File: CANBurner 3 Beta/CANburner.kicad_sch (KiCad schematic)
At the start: 5 parts, among them J1 Conn_02x04_Odd_Even

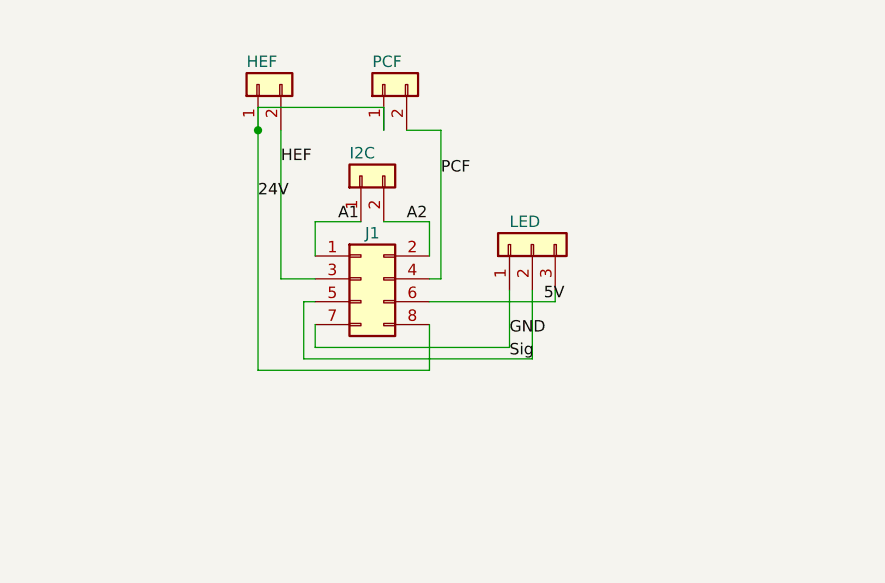
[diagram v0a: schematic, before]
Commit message: Rename KiCAD project files to CANburner
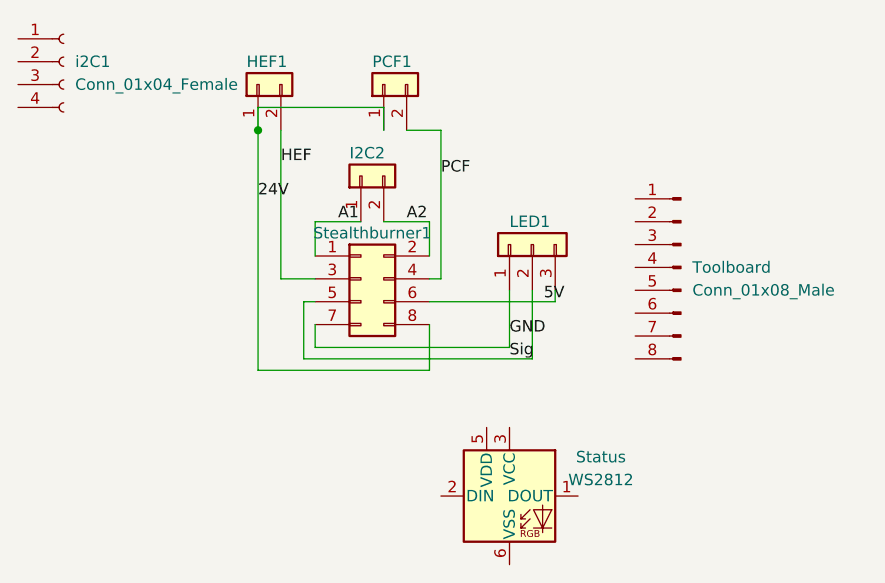
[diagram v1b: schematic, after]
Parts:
- added Status: WS2812, LED_SMD:LED_WS2812_PLCC6_5.0x5.0mm_P1.6mm, symbol LED:WS2812
- added Toolboard: Conn_01x08_Male, Connector_JST:JST_PH_S8B-PH-K_1x08_P2.00mm_Horizontal, symbol Connector:Conn_01x08_Male
- added i2C1: Conn_01x04_Female, Connector_PinSocket_2.54mm:PinSocket_1x04_P2.54mm_Vertical, symbol Connector:Conn_01x04_Female
- renumbered HEF to HEF1, I2C to I2C2, LED to LED1, PCF to PCF1, J1 to Stealthburner1
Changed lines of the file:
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@@
   (symbol (lib_id "Connector_Generic:Conn_02x04_Odd_Even") (at 97.79 91.44 0) (unit 1)
     (in_bom yes) (on_board yes)
-    (property "Reference" "J1" (id 0) (at 99.06 86.36 0))
+    (property "Reference" "Stealthburner1" (id 0) (at 99.06 86.36 0))
     (property "Value" "Conn_02x04_Odd_Even" (id 1) (at 99.06 100.33 0)
       (effects (font (size 1.27 1.27)) hide)
@@
     (pin "8")
   )
+  (symbol (lib_id "LED:WS2812") (at 114.3 115.57 0) (unit 1)
+    (in_bom yes) (on_board yes) (fields_autoplaced)
+    (property "Reference" "Status" (id 0) (at 124.46 111.2393 0))
+    (property "Value" "WS2812" (id 1) (at 124.46 113.7793 0))
+    (property "Footprint" "LED_SMD:LED_WS2812_PLCC6_5.0x5.0mm_P1.6mm" (id 2) (at 115.57 123.19 0)
+      (effects (font (size 1.27 1.27)) (justify left top) hide)
+    )
+    (property "Datasheet" "https://cdn-shop.adafruit.com/datasheets/WS2812.pdf" (id 3) (at 116.84 125.095 0)
+      (effects (font (size 1.27 1.27)) (justify left top) hide)
+    )
+    (pin "1")
+    (pin "2")
+    (pin "3")
+    (pin "4")
+    (pin "5")
+    (pin "6")
+  )
   (symbol (lib_id "Connector_Generic:Conn_01x02") (at 86.36 69.85 90) (unit 1)
     (in_bom yes) (on_board yes)
-    (property "Reference" "HEF" (id 0) (at 85.09 67.31 90)
+    (property "Reference" "HEF1" (id 0) (at 85.09 67.31 90)
       (effects (font (size 1.27 1.27)) (justify right))
     )
@@
   (symbol (lib_id "Connector_Generic:Conn_01x02") (at 97.79 80.01 90) (unit 1)
     (in_bom yes) (on_board yes)
-    (property "Reference" "I2C" (id 0) (at 96.52 77.47 90)
+    (property "Reference" "I2C2" (id 0) (at 96.52 77.47 90)
       (effects (font (size 1.27 1.27)) (justify right))
     )
@@
   (symbol (lib_id "Connector_Generic:Conn_01x03") (at 116.84 87.63 90) (unit 1)
     (in_bom yes) (on_board yes)
-    (property "Reference" "LED" (id 0) (at 114.3 85.09 90)
+    (property "Reference" "LED1" (id 0) (at 114.3 85.09 90)
       (effects (font (size 1.27 1.27)) (justify right))
     )
@@
     (pin "3")
   )
+  (symbol (lib_id "Connector:Conn_01x08_Male") (at 133.35 90.17 0) (mirror y) (unit 1)
+    (in_bom yes) (on_board yes) (fields_autoplaced)
+    (property "Reference" "Toolboard" (id 0) (at 134.62 90.1699 0)
+      (effects (font (size 1.27 1.27)) (justify right))
+    )
+    (property "Value" "Conn_01x08_Male" (id 1) (at 134.62 92.7099 0)
+      (effects (font (size 1.27 1.27)) (justify right))
+    )
+    (property "Footprint" "Connector_JST:JST_PH_S8B-PH-K_1x08_P2.00mm_Horizontal" (id 2) (at 133.35 90.17 0)
+      (effects (font (size 1.27 1.27)) hide)
+    )
+    (property "Datasheet" "~" (id 3) (at 133.35 90.17 0)
+      (effects (font (size 1.27 1.27)) hide)
+    )
+    (pin "1")
+    (pin "2")
+    (pin "3")
+    (pin "4")
+    (pin "5")
+    (pin "6")
+    (pin "7")
+    (pin "8")
+  )
   (symbol (lib_id "Connector_Generic:Conn_01x02") (at 100.33 69.85 90) (unit 1)
     (in_bom yes) (on_board yes)
-    (property "Reference" "PCF" (id 0) (at 99.06 67.31 90)
+    (property "Reference" "PCF1" (id 0) (at 99.06 67.31 90)
       (effects (font (size 1.27 1.27)) (justify right))
     )
@@
     (pin "2")
   )
+  (symbol (lib_id "Connector:Conn_01x04_Female") (at 64.77 67.31 0) (unit 1)
+    (in_bom yes) (on_board yes) (fields_autoplaced)
+    (property "Reference" "i2C1" (id 0) (at 66.04 67.3099 0)
+      (effects (font (size 1.27 1.27)) (justify left))
+    )
+    (property "Value" "Conn_01x04_Female" (id 1) (at 66.04 69.8499 0)
+      (effects (font (size 1.27 1.27)) (justify left))
+    )
+    (property "Footprint" "Connector_PinSocket_2.54mm:PinSocket_1x04_P2.54mm_Vertical" (id 2) (at 64.77 67.31 0)
+      (effects (font (size 1.27 1.27)) hide)
+    )
+    (property "Datasheet" "~" (id 3) (at 64.77 67.31 0)
+      (effects (font (size 1.27 1.27)) hide)
+    )
+    (pin "1")
+    (pin "2")
+    (pin "3")
+    (pin "4")
+  )
   (sheet_instances
     (path "/" (page "1"))
@@
   (symbol_instances
     (path "/5bd3e8e5-fbeb-4d54-b8a6-7d5bfe8d85d0"
-      (reference "HEF") (unit 1) (value "Conn_01x02") (footprint "Connector_JST:JST_XH_B2B-XH-A_1x02_P2.50mm_Vertical")
+      (reference "HEF1") (unit 1) (value "Conn_01x02") (footprint "Connector_JST:JST_XH_B2B-XH-A_1x02_P2.50mm_Vertical")
     )
     (path "/75a21d3e-adda-4162-89d2-033dbb93e6a2"
-      (reference "I2C") (unit 1) (value "Conn_01x02") (footprint "Connector_JST:JST_XH_B2B-XH-A_1x02_P2.50mm_Vertical")
+      (reference "I2C2") (unit 1) (value "Conn_01x02") (footprint "Connector_JST:JST_XH_B2B-XH-A_1x02_P2.50mm_Vertical")
+    )
+    (path "/9f8f78d8-da39-4e4f-b694-a9a2d22b21ca"
+      (reference "LED1") (unit 1) (value "Conn_01x03") (footprint "Connector_JST:JST_XH_B3B-XH-A_1x03_P2.50mm_Vertical")
+    )
+    (path "/cc3d9eca-cc0e-4e40-a51e-30dcd8f4b078"
+      (reference "PCF1") (unit 1) (value "Conn_01x02") (footprint "Connector_JST:JST_XH_B2B-XH-A_1x02_P2.50mm_Vertical")
+    )
+    (path "/2d3de8b5-2057-4592-9199-6204fc470f86"
+      (reference "Status") (unit 1) (value "WS2812") (footprint "LED_SMD:LED_WS2812_PLCC6_5.0x5.0mm_P1.6mm")
     )
     (path "/27ab04c7-a94a-4111-8751-a5990e293b34"
-      (reference "J1") (unit 1) (value "Conn_02x04_Odd_Even") (footprint "Connector_PinHeader_2.54mm:PinHeader_2x04_P2.54mm_Horizontal")
+      (reference "Stealthburner1") (unit 1) (value "Conn_02x04_Odd_Even") (footprint "Connector_PinHeader_2.54mm:PinHeader_2x04_P2.54mm_Horizontal")
     )
-    (path "/9f8f78d8-da39-4e4f-b694-a9a2d22b21ca"
-      (reference "LED") (unit 1) (value "Conn_01x03") (footprint "Connector_JST:JST_XH_B3B-XH-A_1x03_P2.50mm_Vertical")
+    (path "/c55470b2-8c06-49a0-900e-c027ebc34036"
+      (reference "Toolboard") (unit 1) (value "Conn_01x08_Male") (footprint "Connector_JST:JST_PH_S8B-PH-K_1x08_P2.00mm_Horizontal")
     )
-    (path "/cc3d9eca-cc0e-4e40-a51e-30dcd8f4b078"
-      (reference "PCF") (unit 1) (value "Conn_01x02") (footprint "Connector_JST:JST_XH_B2B-XH-A_1x02_P2.50mm_Vertical")
+    (path "/cd2825df-2c84-4771-afa6-21b362c90345"
+      (reference "i2C1") (unit 1) (value "Conn_01x04_Female") (footprint "Connector_PinSocket_2.54mm:PinSocket_1x04_P2.54mm_Vertical")
     )
   )
